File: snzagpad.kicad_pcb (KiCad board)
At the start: 2 copper layers, 76.2 x 100.6 mm, 79 parts, among them J1 USB_C, J3 SWD, SW0 Boot, SW1 ?, SW10 ?, SW11 ?, SW12 ?, SW13 ?, SW14 ?, SW15 ?, SW16 ?, SW17 ?, SW18 ?, SW19 ?, SW2 ?, SW20 ?, SW21 ?, SW22 ?, SW23 ?, SW3 ?, SW4 ?, SW5 ?, SW6 ?, SW7 ?, SW8 ?, SW9 ?, U1 RP2040, U2 SRV05-4, U3 XC6206, U4 W25Q128JVS, Y1 12MHz

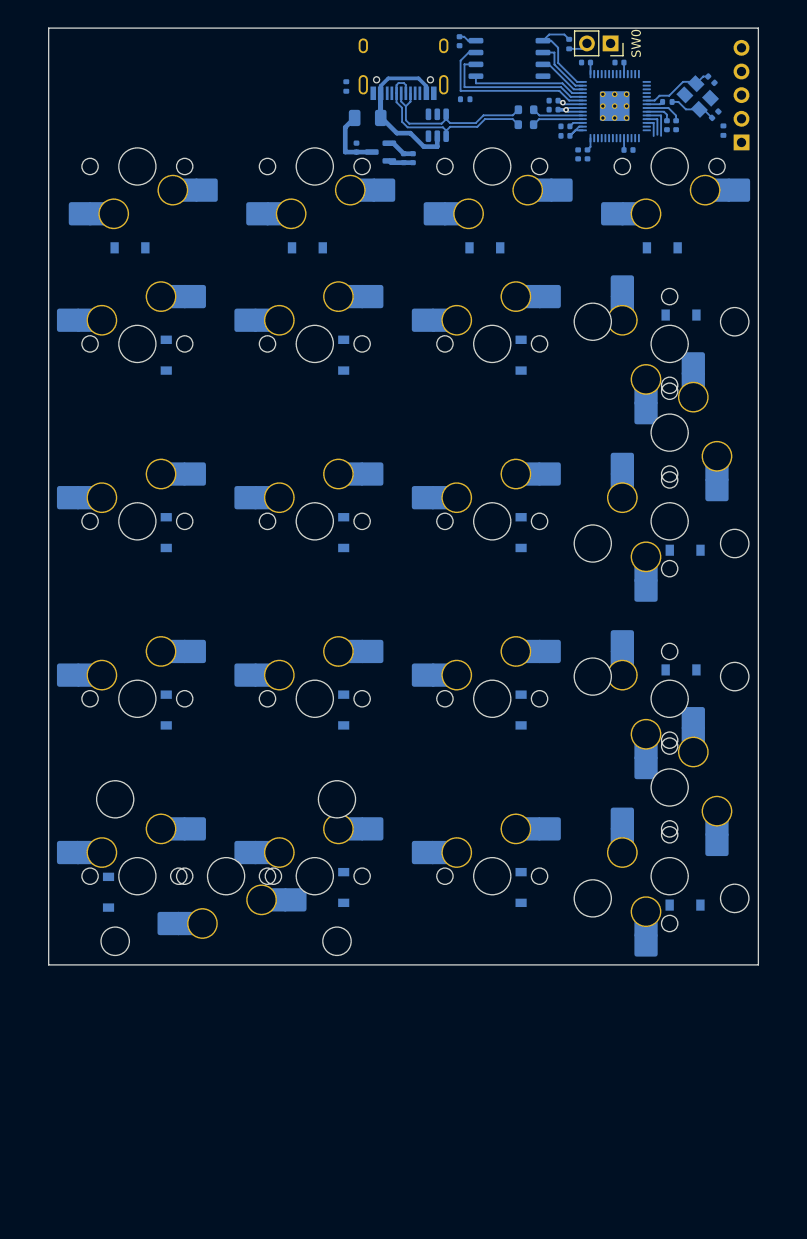
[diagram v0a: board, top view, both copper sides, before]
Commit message: Updated outline, added mounts, preliminary routing
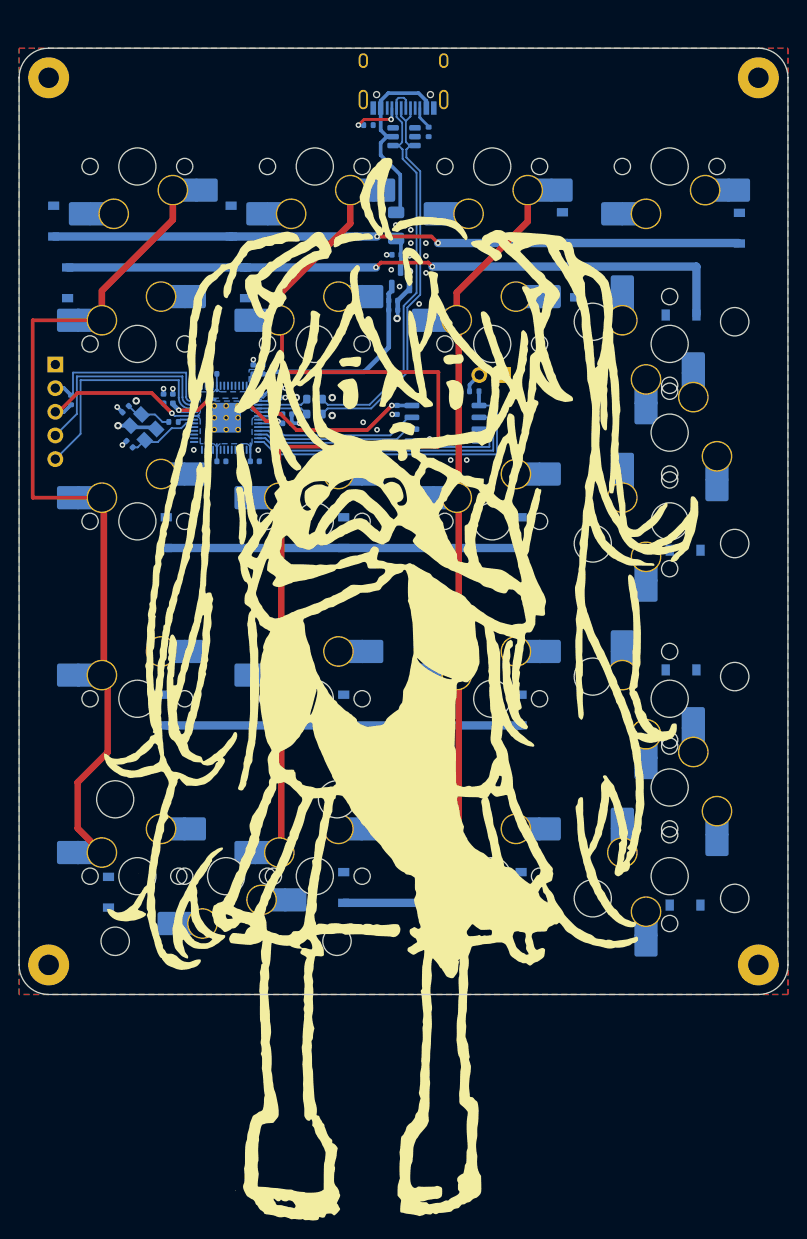
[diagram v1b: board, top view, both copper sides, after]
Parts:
- added G***: LOGO, LOGO, F.Cu at (69.5, 119.3)
- added H1: MP, MountingHole:MountingHole_2.2mm_M2_Pad, B.Cu at (32.5, 52.4)
- added H2: MP, MountingHole:MountingHole_2.2mm_M2_Pad, B.Cu at (108.7, 52.4)
- added H3: MP, MountingHole:MountingHole_2.2mm_M2_Pad, B.Cu at (32.5, 147.6)
- added H4: MP, MountingHole:MountingHole_2.2mm_M2_Pad, B.Cu at (108.7, 147.6)
- J2: renamed from J3; moved to F.Cu
- moved J2 77.4 mm to (33.3, 83.2)
- moved R1 75.8 mm to (34.9, 87.0)
- moved C15 73.7 mm to (41.2, 91.7), turned to -45 degrees
- moved C16 70.8 mm to (40.8, 88.0), turned to 45 degrees
- moved Y1 69.3 mm to (42.7, 89.9), turned to -45 degrees
- moved R6 63.2 mm to (45.9, 89.3), turned to 0 degrees
- moved C13 62.4 mm to (44.9, 86.8), turned to 90 degrees
- moved C2 60.6 mm to (45.9, 86.8), turned to 90 degrees
- moved C9 60.5 mm to (51.1, 93.6), turned to 0 degrees
- moved C11 55.7 mm to (54.7, 93.6), turned to 0 degrees
- moved U2 53.5 mm to (51.6, 88.9), turned to 90 degrees
- moved C17 50.7 mm to (50.1, 84.2), turned to 180 degrees
- moved C3 44.9 mm to (58.2, 89.5), turned to 0 degrees
- moved C14 43.4 mm to (58.2, 88.5), turned to 0 degrees
- moved C10 42.7 mm to (54.5, 83.7), turned to 90 degrees
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- renumbered C10 to C1, C12 to C10, C14 to C11, C15 to C12, C16 to C13, C17 to C14, C1 to C15, C2 to C16, C5 to C17, C11 to C2, C13 to C3, C3 to C4, C4 to C5, D11 to D10, D12 to D11, D13 to D12, D14 to D13, D15 to D14, D16 to D15, D17 to D16, D19 to D17, D21 to D18, D22 to D19, D23 to D20, D10 to D9, R3 to R1, R4 to R2, R5 to R3, R1 to R4, R2 to R5, R7 to R6, R6 to R7, S9 to S1, S20 to S2, S22 to S3, SW0 to SW24, U3 to U1, U1 to U2, U2 to U3
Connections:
- J2 pad 2: +3V3 -> ~{RESET}
- J2 pad 3: ~{RESET} -> +3V3
- J2 pad 4: SWCLK -> SWD
- J2 pad 5: SWD -> SWCLK
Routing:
- net COL1: track 0.00 -> 108.6 mm
- net COL0: track 0.00 -> 92.0 mm
- net COL2: track 0.00 -> 74.8 mm
- net ROW0: track 0.00 -> 73.9 mm, vias 0 -> 2
- net ROW1: track 0.00 -> 73.1 mm, vias 0 -> 2
- net +3V3: track 21.8 -> 76.6 mm, vias 1 -> 3
- net ROW3: track 0.00 -> 38.1 mm
- net ROW2: track 0.00 -> 38.1 mm
- net DBUS+: track 18.9 -> 43.8 mm
- net CS: track 10.4 -> 34.9 mm
- net SD1: track 6.49 -> 30.9 mm
- net DBUS-: track 21.1 -> 44.6 mm
- net SD2: track 5.37 -> 28.4 mm
- net SWCLK: track 3.73 -> 24.3 mm
- net SWD: track 2.82 -> 22.6 mm
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- added copper zone on B.Cu, net +1V1
- added copper zone on B.Cu, net +3V3
- added copper zone on B.Cu, net GND
- added copper zone on F.Cu, net GND
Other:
- board size 76.2 x 100.6 mm -> 82.6 x 101.6 mm

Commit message: Edited cutout, mounts, USB position, routing
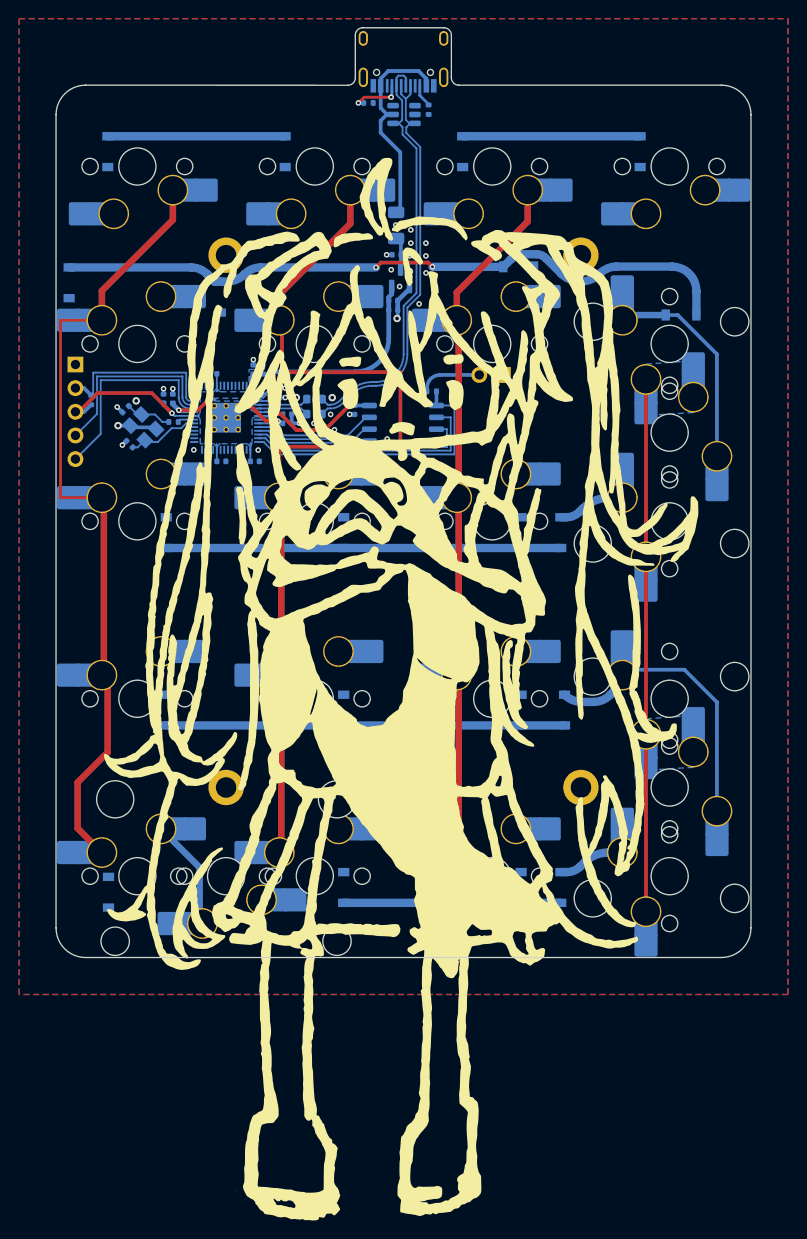
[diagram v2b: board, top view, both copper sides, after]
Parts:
- H1, H2, H3, H4: footprint MountingHole:MountingHole_2.2mm_M2_Pad -> MountingHole:MountingHole_2.2mm_M2_ISO14580_Pad
- moved H2 26.9 mm to (89.7, 71.4)
- moved H1 26.9 mm to (51.6, 71.4)
- moved H4 26.9 mm to (89.7, 128.6)
- moved H3 26.9 mm to (51.6, 128.6)
- moved D12 13.5 mm to (87.5, 101.2), turned to 90 degrees
- moved D20 13.5 mm to (87.5, 139.3), turned to 90 degrees
- moved D3 13.5 mm to (77.0, 60.3), turned to -90 degrees
- moved D4 13.5 mm to (96.0, 60.3), turned to -90 degrees
- moved D16 13.2 mm to (87.9, 120.3), turned to 90 degrees
- moved D1 9.45 mm to (38.9, 60.3), turned to -90 degrees
- moved D2 9.45 mm to (57.9, 60.3), turned to -90 degrees
- moved D7 6.32 mm to (83.0, 72.7), turned to 0 degrees
- moved U4 4.57 mm to (70.6, 89.5)
- moved C12 4.57 mm to (65.4, 88.1)
- moved R7 4.57 mm to (73.7, 86.1)
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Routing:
- net COL3: track 0.00 -> 57.2 mm
- net ROW0: track 73.9 -> 38.1 mm, vias 2 -> 0
- net Net-(D16-Pad2): track 0.00 -> 31.5 mm
- net Net-(D8-Pad2): track 0.00 -> 23.1 mm
- net Net-(D17-Pad2): track 0.00 -> 12.0 mm
- net COL1: track 108.6 -> 100.5 mm
- net Net-(D20-Pad2): track 0.00 -> 7.20 mm
- net Net-(D12-Pad2): track 0.00 -> 7.19 mm
- net +3V3: track 76.6 -> 69.7 mm
- net COL0: track 92.0 -> 86.0 mm
- net ROW3: track 38.1 -> 42.8 mm
- net SD2: track 28.4 -> 23.8 mm
- net SD0: track 17.1 -> 12.6 mm
- net SD3: track 17.8 -> 13.3 mm
- net SD1: track 30.9 -> 26.3 mm
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- added copper zone on B.Cu, net COL3
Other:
- board size 82.6 x 101.6 mm -> 74.6 x 99.8 mm

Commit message: Completed mostly, rounded traces, connected everything
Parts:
- moved G*** 12.7 mm to (71.2, 106.7)
- moved C9 0.81 mm to (50.4, 94.0), turned to -90 degrees
- moved C11 0.21 mm to (54.9, 93.5)
- moved C17 0.20 mm to (49.9, 84.2)
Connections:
- SW19 pad 1: COL0 -> Net-(D17-Pad2)
- SW19 pad 2: Net-(D17-Pad2) -> COL0
- SW20 pad 1: COL0 -> Net-(D17-Pad2)
- SW20 pad 2: Net-(D17-Pad2) -> COL0
- U2 pad 2: unconnected-(U2-Pad2) -> ROW4
- U2 pad 3: unconnected-(U2-Pad3) -> ROW3
- U2 pad 34: unconnected-(U2-Pad34) -> ROW1
- U2 pad 35: unconnected-(U2-Pad35) -> ROW0
- U2 pad 4: unconnected-(U2-Pad4) -> ROW2
- U2 pad 5: unconnected-(U2-Pad5) -> COL3
- U2 pad 6: unconnected-(U2-Pad6) -> COL2
- U2 pad 7: unconnected-(U2-Pad7) -> COL1
- U2 pad 8: unconnected-(U2-Pad8) -> COL0
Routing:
- net COL3: track 57.2 -> 146.4 mm
- net ROW4: track 23.3 -> 110.5 mm, vias 0 -> 2
- net ROW0: track 38.1 -> 86.9 mm, vias 0 -> 4
- net COL2: track 74.8 -> 122.7 mm
- net ROW3: track 42.8 -> 82.3 mm, vias 0 -> 2
- net COL0: track 86.0 -> 124.6 mm
- net COL1: track 100.5 -> 124.6 mm
- net ROW1: track 76.1 -> 90.2 mm, vias 2 -> 4
- net Net-(D6-Pad2): track 0.00 -> 13.8 mm
- net ROW2: track 42.4 -> 55.9 mm, vias 0 -> 3
- net Net-(D5-Pad2): track 0.00 -> 10.3 mm
- net GND: track 16.0 -> 25.6 mm, vias 31 -> 122
- net Net-(D17-Pad2): track 12.0 -> 20.7 mm
- net Net-(D1-Pad2): track 0.00 -> 5.28 mm
- net Net-(D2-Pad2): track 0.00 -> 5.28 mm
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
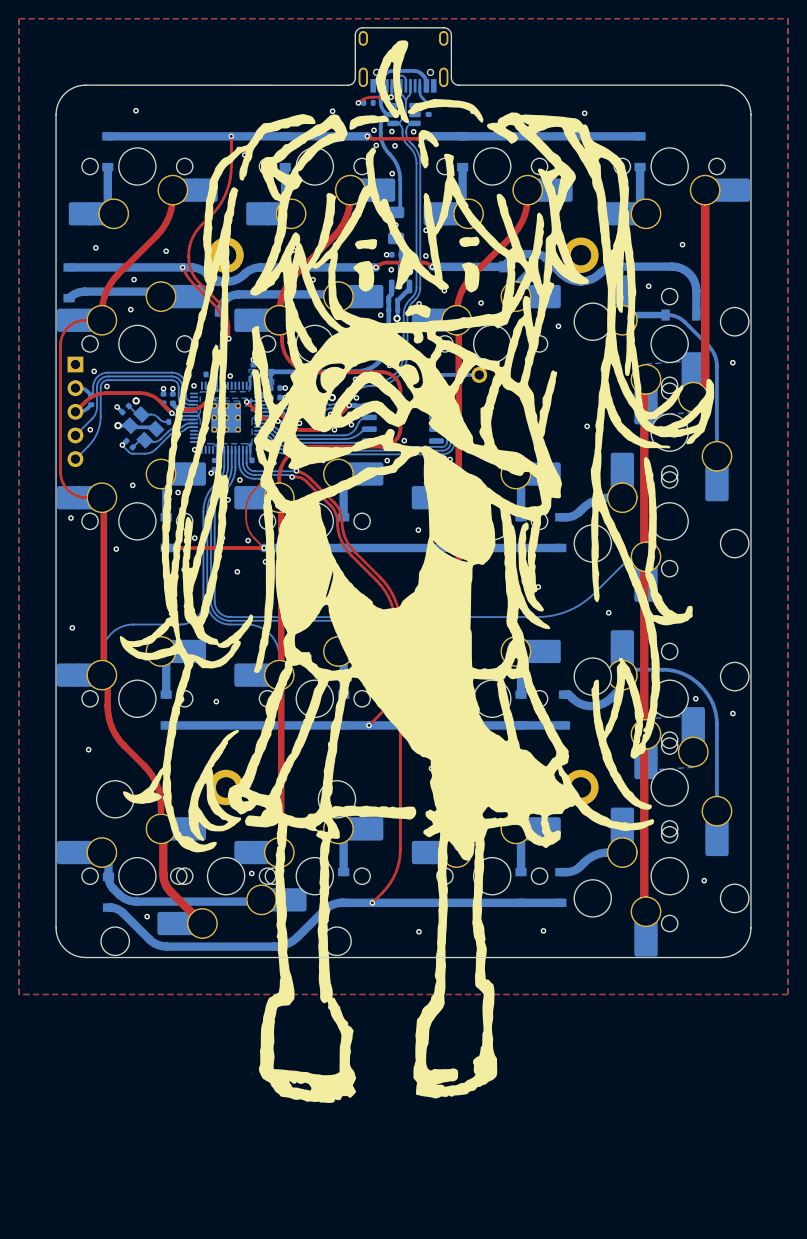
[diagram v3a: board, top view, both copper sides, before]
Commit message: Updated outline, more silkscreens
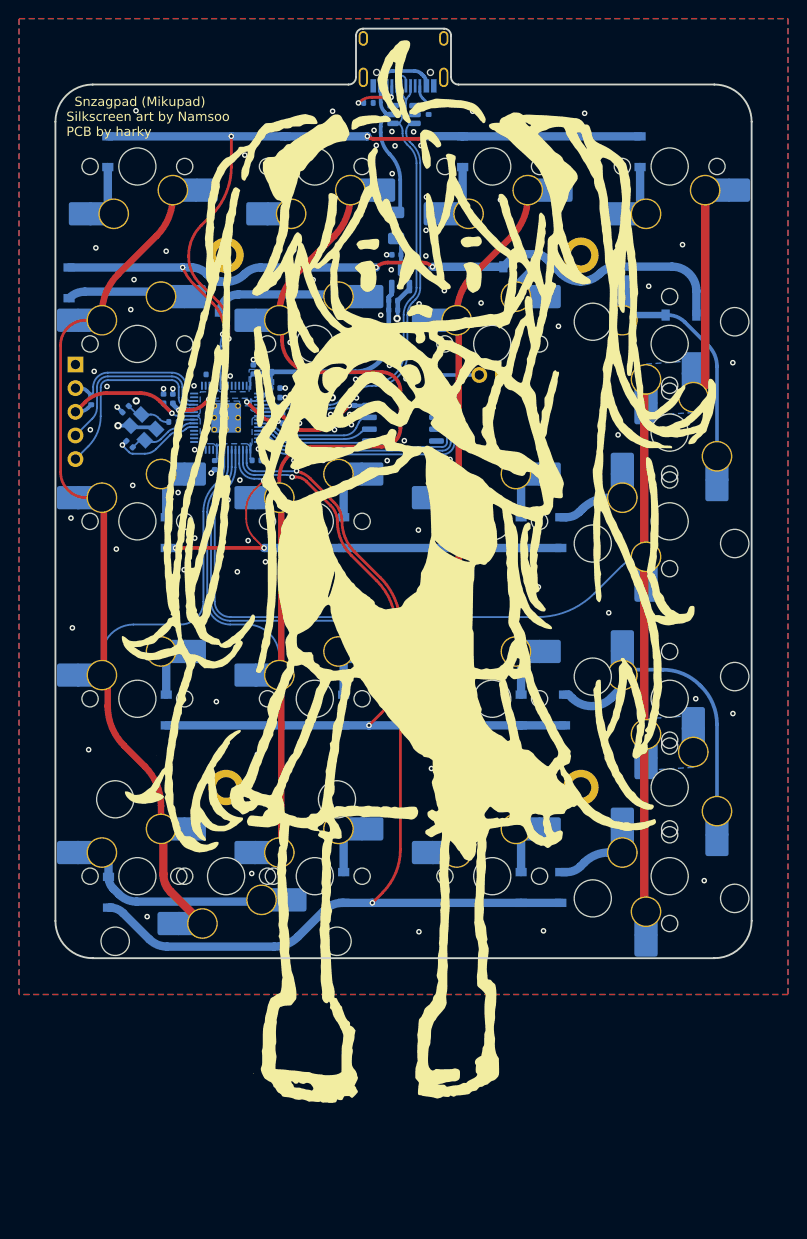
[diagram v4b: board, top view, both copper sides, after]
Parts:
- removed the G*** at (71.2, 106.7)
- added G***: LOGO, LOGO, F.Cu at (71.4, 106.7)
- added G***: LOGO, LOGO, B.Cu at (87.0, 87.5)
- added G***: LOGO, LOGO, B.Cu at (38.7, 107.2)
- added G***: LOGO, LOGO, B.Cu at (53.8, 106.7)
- added G***: LOGO, LOGO, B.Cu at (74.0, 126.6)
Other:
- board size 74.6 x 99.8 mm -> 74.8 x 99.8 mm
- board text added: "Snzagpad (Mikupad) Silkscreen art by Namsoo PCB by harky"
- board text added: "Snzagpad Proto For Snzag Keys. https://github.com/zykrah/snzagpad © Zykrah 2022"

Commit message: More silkscreen additions/modification, added teardrops
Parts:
- removed the G*** at (53.8, 106.7)
- added G***: LOGO, LOGO, B.Cu at (103.8, 109.8)
- added G***: LOGO, LOGO, B.Cu at (72.4, 106.1)
- added G***: LOGO, LOGO, B.Cu at (104.5, 144.7)
- added G***: LOGO, LOGO, B.Cu at (89.3, 57.5)
- added G***: LOGO, LOGO, B.Cu at (49.5, 57.2)
- added G***: LOGO, LOGO, B.Cu at (45.2, 126.7)
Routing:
- net ROW2: track 55.9 -> 57.6 mm
- net COL3: track 146.4 -> 147.6 mm
- net COL2: track 122.7 -> 121.7 mm
- net GND: vias 122 -> 123
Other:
- board text added: "3V3"
- board text added: "BOOT"
- board text added: "GND"
- board text added: "RST"
- board text added: "SCK"
- board text added: "SWD"
- board text added: "Snzagpad Proto For Snzag Keys © Zykrah 2022"
- board text added: "art cred: snag - ok.png donut - lissy thank you"
- board text removed: "Snzagpad Proto For Snzag Keys. https://github.com/zykrah/snzagpad © Zykrah 2022"
